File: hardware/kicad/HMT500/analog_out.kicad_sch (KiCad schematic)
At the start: 20 parts, among them U10 TPS26611, U7 DAC8760IPWP, U8 DAC8760IPWP, U9 TPS26611

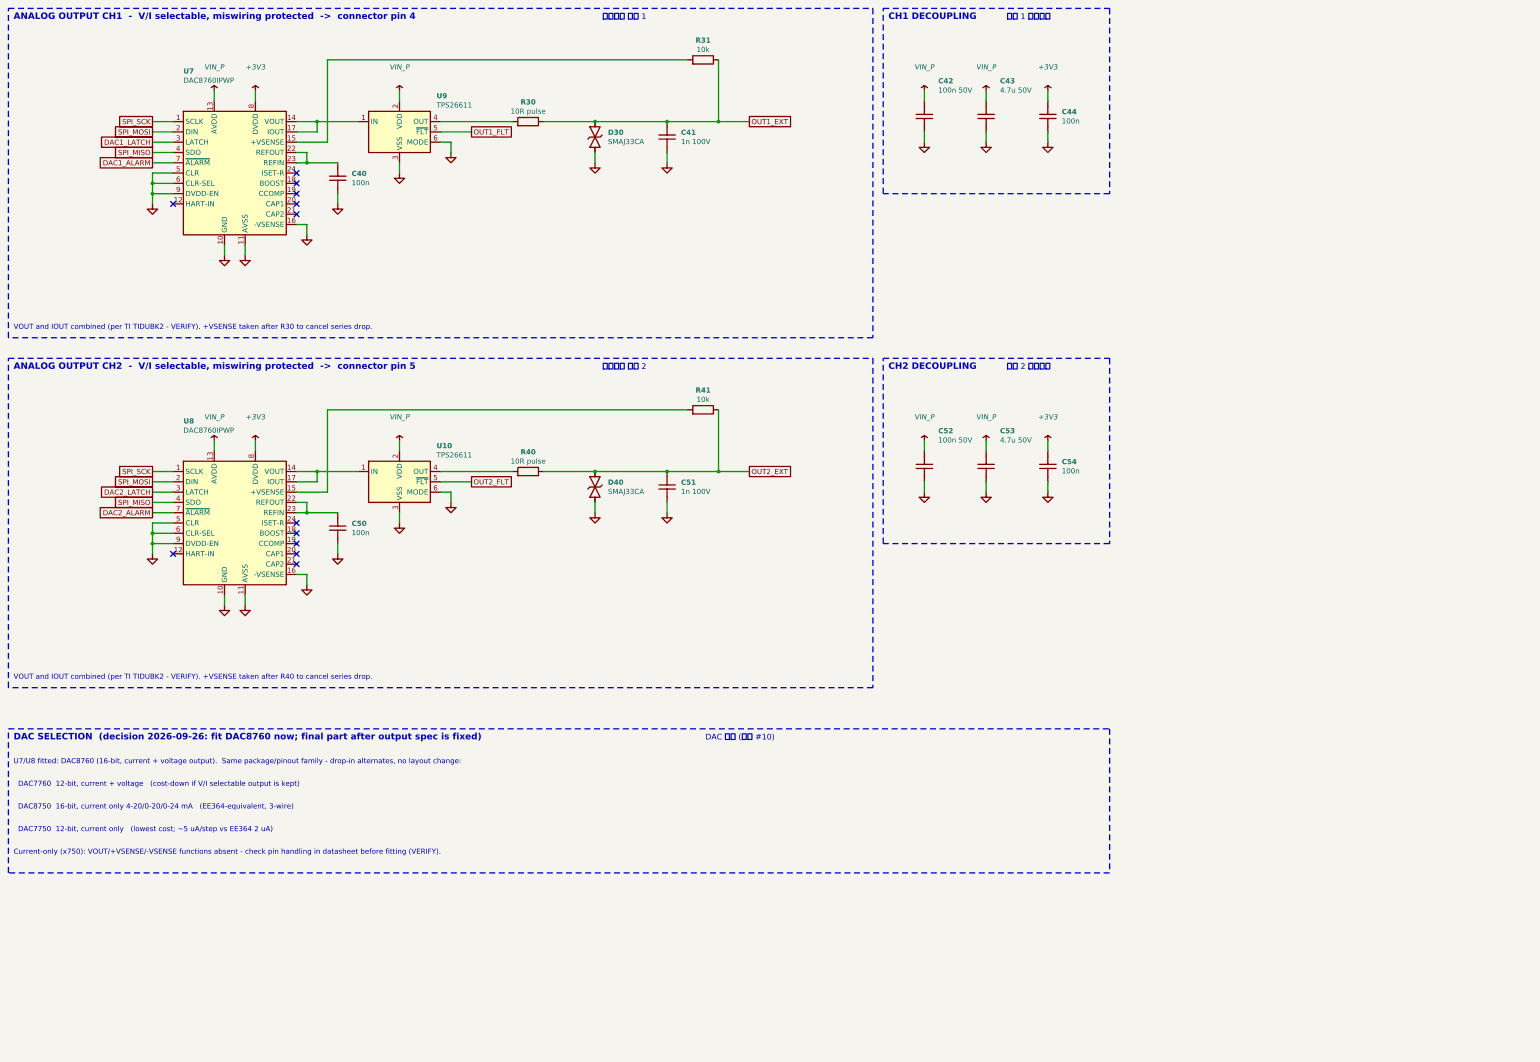
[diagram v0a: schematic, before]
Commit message: Schematic redraw: aligned parts, straight wires, fewer junctions
- Bends 54 -> 1, junctions 51 -> 31 (remaining are real 3-way nodes: divider taps,
  protection taps, tied pin pairs, power flags)
- Power pins get their own power symbols instead of rails with T-branches; signals
  between distant parts use labels; two-pin parts sit on the pin row they connect to
- Symbol pin order rearranged for straight runs (pin numbers unchanged): TPS2660,
  LMR36006 (BOOT on top), PCAP04 (Cref pins 3 rows apart, VDD18 on right), ADS1220
  (bottom pins 3 apart), DAC8760 (GND-tied pins on bottom), TPS26611 (FLT on bottom)
- New checks: pin names inside IC bodies must not overlap, boxes must not overlap;
  test limits bends per sheet and total junctions
- Netlist check 63 nets, 0 errors

Co-Authored-By: Claude Opus 5.5 <noreply@anthropic.com>
Claude-Session: https://claude.ai/code/session_01JA2o8uJsqp9Vzsg4b665ev
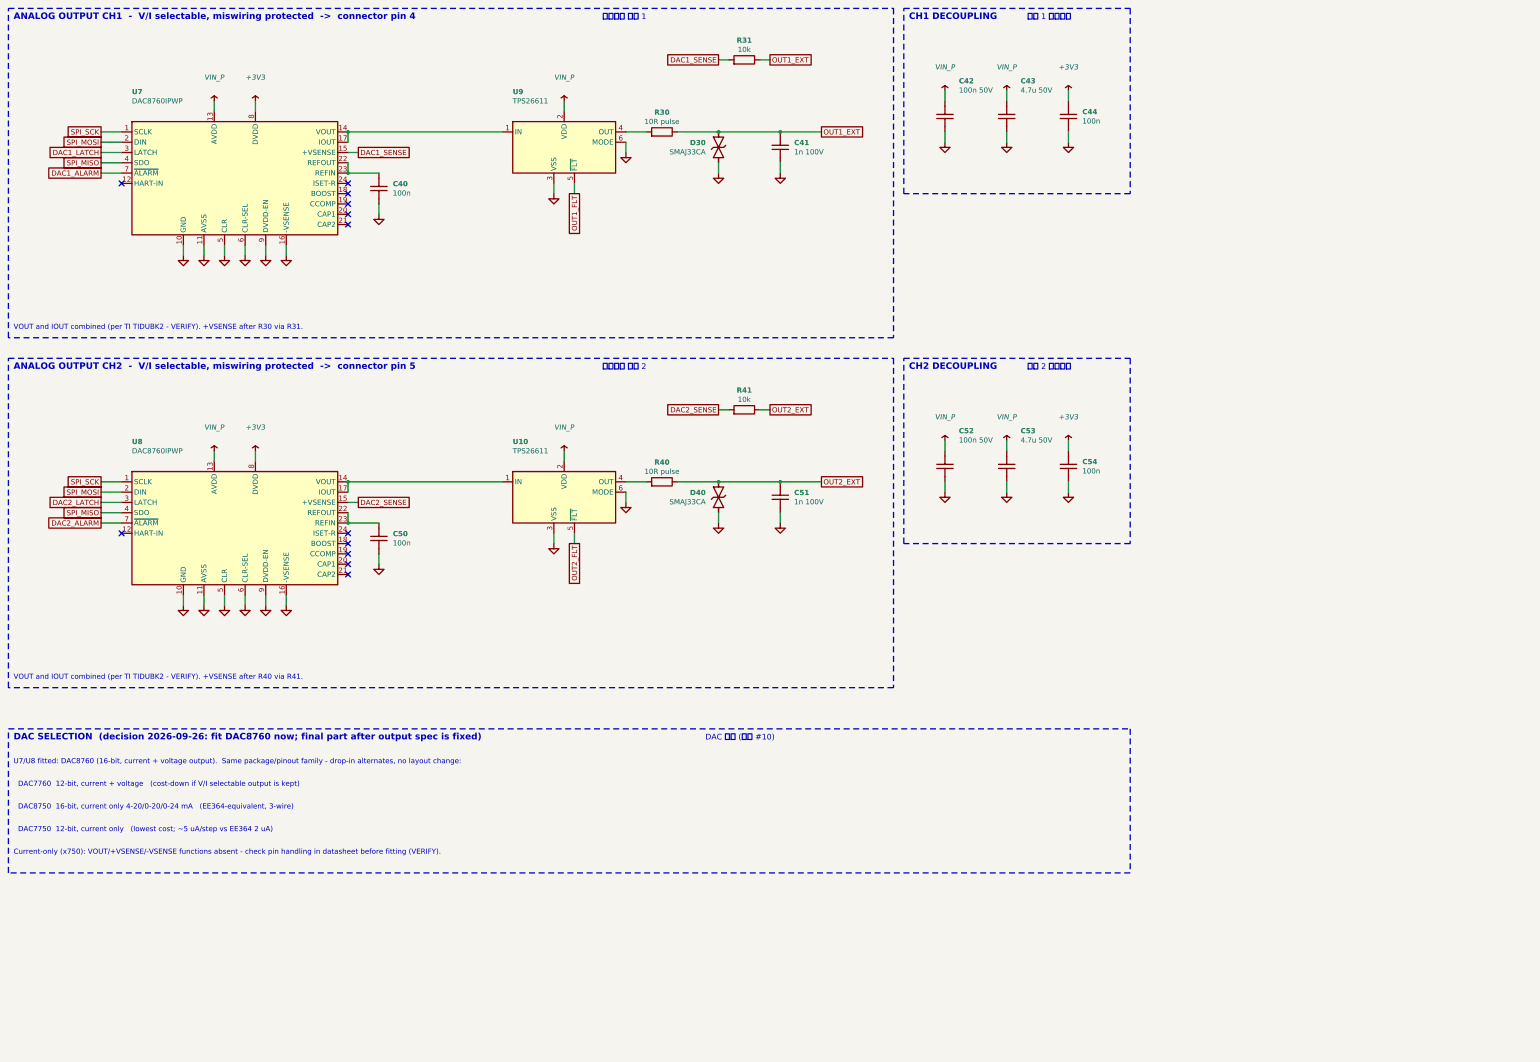
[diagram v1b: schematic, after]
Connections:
- net DAC1_SENSE: now reaches R31.1, U7.15 (+VSENSE)
- net DAC2_SENSE: now reaches R41.1, U8.15 (+VSENSE)
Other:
- note added: "VOUT and IOUT combined (per TI TIDUBK2 - VERIFY). +VSENSE after R30 via R31."
- note added: "VOUT and IOUT combined (per TI TIDUBK2 - VERIFY). +VSENSE after R40 via R41."
- note removed: "VOUT and IOUT combined (per TI TIDUBK2 - VERIFY). +VSENSE taken after R30 to cancel series drop."
- note removed: "VOUT and IOUT combined (per TI TIDUBK2 - VERIFY). +VSENSE taken after R40 to cancel series drop."
- moved on the sheet: C40, C41, C42, C43, C44, C50, C51, C52, C53, C54, D30, D40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

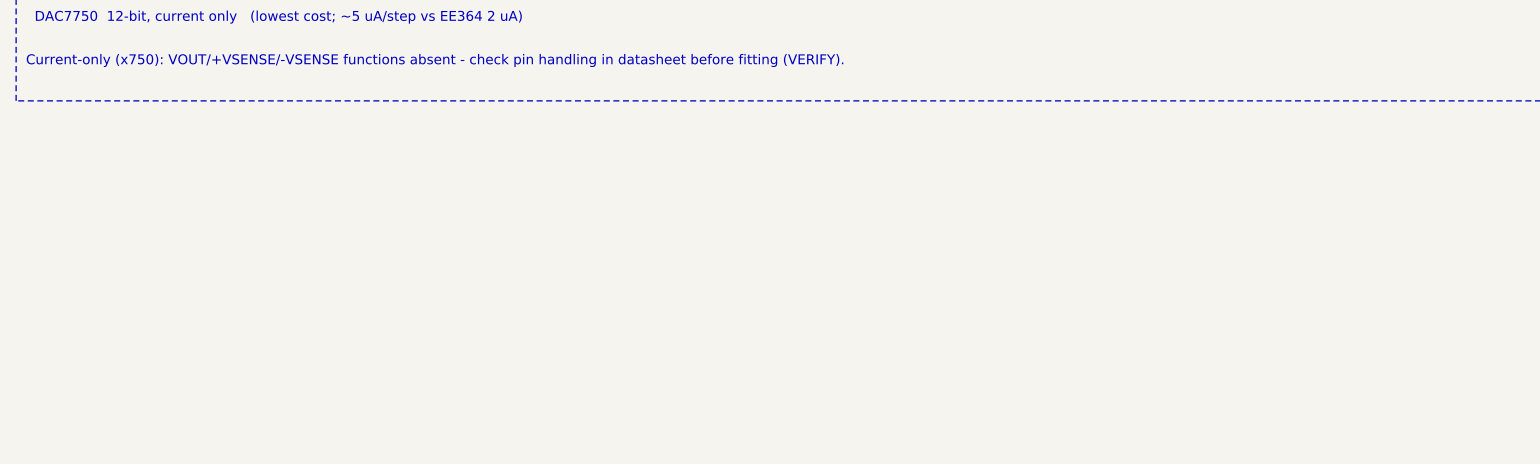
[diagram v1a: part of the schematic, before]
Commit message: Schematic: key-parts table (role, features, specs) on every sheet
- Aligned 4-column table per sheet: reference, part, role, features/specs;
  values still to confirm against datasheets marked with *
- Connector and RS-485 sheets moved to A3 for room
- New checks: text and boxes stay inside the page and out of the title block;
  every character of Hangul text must exist in NanumGothic (minus sign and micro
  sign substituted)

Co-Authored-By: Claude Opus 5.5 <noreply@anthropic.com>
Claude-Session: https://claude.ai/code/session_01JA2o8uJsqp9Vzsg4b665ev
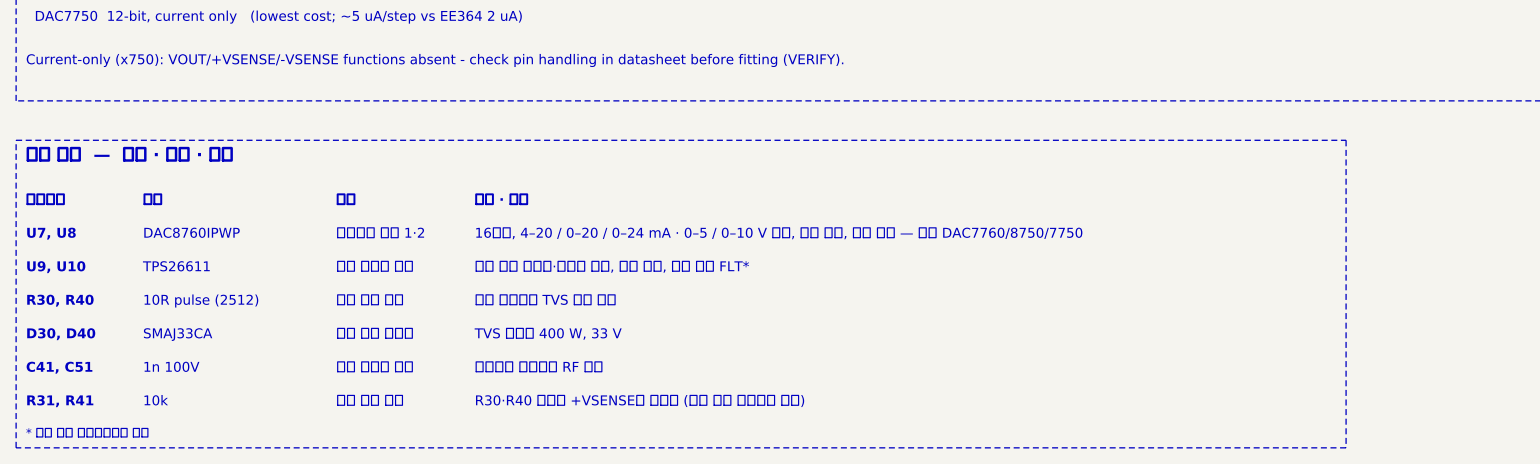
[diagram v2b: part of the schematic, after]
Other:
- note added: "* 표시 값은 데이터시트로 확인"
- note added: "10R pulse (2512)"
- note added: "10k"
- note added: "16비트, 4–20 / 0–20 / 0–24 mA · 0–5 / 0–10 V 선택, 내부 기준, 고장 알람 — 대체 DAC7760/8750/7750"
- note added: "1n 100V"
- note added: "C41, C51"
- note added: "D30, D40"
- note added: "DAC8760IPWP"
- note added: "R30, R40"
- note added: "R30·R40 뒤에서 +VSENSE로 되먹임 (직렬 저항 전압강하 보상)"
- note added: "R31, R41"
- note added: "SMAJ33CA"
- note added: "TPS26611"
- note added: "TVS 양방향 400 W, 33 V"
- note added: "U7, U8"
- note added: "U9, U10"
- note added: "부품"
- note added: "부품번호"
- note added: "서지 전류 제한"
- note added: "아날로그 출력 1·2"
- note added: "역할"
- note added: "전압 출력 감지"
- note added: "주요 부품 — 역할 · 특징 · 사양"
- note added: "출력 고주파 필터"
- note added: "출력 단자 과전압·역전압 차단, 전류 제한, 고장 출력 FLT*"
- note added: "출력 보호기와 TVS 사이 직렬"
- note added: "출력 서지 클램프"
- note added: "출력 오결선 보호"
- note added: "케이블로 들어오는 RF 억제"
- note added: "특징 · 사양"
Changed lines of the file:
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@@
 (rectangle (start 251.46 101.6) (end 307.34 147.32) (stroke (width 0.1524) (type dash) (color 72 72 160 1)) (fill (type none)))
 (rectangle (start 30.48 193.04) (end 307.34 228.6) (stroke (width 0.1524) (type dash) (color 72 72 160 1)) (fill (type none)))
+(rectangle (start 30.48 233.68) (end 201.831 273.304) (stroke (width 0.1524) (type dash) (color 72 72 160 1)) (fill (type none)))
 (text "ANALOG OUTPUT CH1  -  V/I selectable, miswiring protected  ->  connector pin 4" (at 31.75 18.288 0) (effects (font (size 1.6 1.6) bold) (justify left bottom)))
 (text "아날로그 출력 1" (at 177.083 18.288 0) (effects (font (face "NanumGothic") (size 1.4 1.4)) (justify left bottom)))
@@
 (text "  DAC7750  12-bit, current only   (lowest cost; ~5 uA/step vs EE364 2 uA)" (at 31.75 218.694 0) (effects (font (size 1.27 1.27)) (justify left bottom)))
 (text "Current-only (x750): VOUT/+VSENSE/-VSENSE functions absent - check pin handling in datasheet before fitting (VERIFY)." (at 31.75 224.282 0) (effects (font (size 1.27 1.27)) (justify left bottom)))
+(text "부품번호" (at 31.75 242.316 0) (effects (font (face "NanumGothic") (size 1.27 1.27) bold) (justify left bottom)))
+(text "부품" (at 46.8274 242.316 0) (effects (font (face "NanumGothic") (size 1.27 1.27) bold) (justify left bottom)))
+(text "역할" (at 71.7194 242.316 0) (effects (font (face "NanumGothic") (size 1.27 1.27) bold) (justify left bottom)))
+(text "특징 · 사양" (at 89.5629 242.316 0) (effects (font (face "NanumGothic") (size 1.27 1.27) bold) (justify left bottom)))
+(text "U7, U8" (at 31.75 246.634 0) (effects (font (size 1.27 1.27) bold) (justify left bottom)))
+(text "DAC8760IPWP" (at 46.8274 246.634 0) (effects (font (size 1.27 1.27)) (justify left bottom)))
+(text "아날로그 출력 1·2" (at 71.7194 246.634 0) (effects (font (face "NanumGothic") (size 1.27 1.27)) (justify left bottom)))
+(text "16비트, 4–20 / 0–20 / 0–24 mA · 0–5 / 0–10 V 선택, 내부 기준, 고장 알람 — 대체 DAC7760/8750/7750" (at 89.5629 246.634 0) (effects (font (face "NanumGothic") (size 1.27 1.27)) (justify left bottom)))
+(text "U9, U10" (at 31.75 250.952 0) (effects (font (size 1.27 1.27) bold) (justify left bottom)))
+(text "TPS26611" (at 46.8274 250.952 0) (effects (font (size 1.27 1.27)) (justify left bottom)))
+(text "출력 오결선 보호" (at 71.7194 250.952 0) (effects (font (face "NanumGothic") (size 1.27 1.27)) (justify left bottom)))
+(text "출력 단자 과전압·역전압 차단, 전류 제한, 고장 출력 FLT*" (at 89.5629 250.952 0) (effects (font (face "NanumGothic") (size 1.27 1.27)) (justify left bottom)))
+(text "R30, R40" (at 31.75 255.27 0) (effects (font (size 1.27 1.27) bold) (justify left bottom)))
+(text "10R pulse (2512)" (at 46.8274 255.27 0) (effects (font (size 1.27 1.27)) (justify left bottom)))
+(text "서지 전류 제한" (at 71.7194 255.27 0) (effects (font (face "NanumGothic") (size 1.27 1.27)) (justify left bottom)))
+(text "출력 보호기와 TVS 사이 직렬" (at 89.5629 255.27 0) (effects (font (face "NanumGothic") (size 1.27 1.27)) (justify left bottom)))
+(text "D30, D40" (at 31.75 259.588 0) (effects (font (size 1.27 1.27) bold) (justify left bottom)))
+(text "SMAJ33CA" (at 46.8274 259.588 0) (effects (font (size 1.27 1.27)) (justify left bottom)))
+(text "출력 서지 클램프" (at 71.7194 259.588 0) (effects (font (face "NanumGothic") (size 1.27 1.27)) (justify left bottom)))
+(text "TVS 양방향 400 W, 33 V" (at 89.5629 259.588 0) (effects (font (face "NanumGothic") (size 1.27 1.27)) (justify left bottom)))
+(text "C41, C51" (at 31.75 263.906 0) (effects (font (size 1.27 1.27) bold) (justify left bottom)))
+(text "1n 100V" (at 46.8274 263.906 0) (effects (font (size 1.27 1.27)) (justify left bottom)))
+(text "출력 고주파 필터" (at 71.7194 263.906 0) (effects (font (face "NanumGothic") (size 1.27 1.27)) (justify left bottom)))
+(text "케이블로 들어오는 RF 억제" (at 89.5629 263.906 0) (effects (font (face "NanumGothic") (size 1.27 1.27)) (justify left bottom)))
+(text "R31, R41" (at 31.75 268.224 0) (effects (font (size 1.27 1.27) bold) (justify left bottom)))
+(text "10k" (at 46.8274 268.224 0) (effects (font (size 1.27 1.27)) (justify left bottom)))
+(text "전압 출력 감지" (at 71.7194 268.224 0) (effects (font (face "NanumGothic") (size 1.27 1.27)) (justify left bottom)))
+(text "R30·R40 뒤에서 +VSENSE로 되먹임 (직렬 저항 전압강하 보상)" (at 89.5629 268.224 0) (effects (font (face "NanumGothic") (size 1.27 1.27)) (justify left bottom)))
+(text "주요 부품  —  역할 · 특징 · 사양" (at 31.75 236.728 0) (effects (font (face "NanumGothic") (size 1.6 1.6) bold) (justify left bottom)))
+(text "* 표시 값은 데이터시트로 확인" (at 31.75 272.288 0) (effects (font (face "NanumGothic") (size 1.1 1.1)) (justify left bottom)))
 )
